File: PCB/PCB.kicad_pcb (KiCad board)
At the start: 2 copper layers, 266.7 x 76.2 mm, 122 parts, among them J1 USB-C USB 2.0 MC-372, J2 Conn_01x04, J3 Conn_01x02, Q1 AO3407, Q2 AO3406, SW1 SW_Push, SW10 SW_Push, SW11 SW_Push, SW12 SW_Push, SW13 SW_Push, SW14 SW_Push, SW15 SW_Push, SW16 SW_Push, SW17 SW_Push, SW18 SW_Push, SW19 SW_Push, SW2 SW_Push, SW20 SW_Push, SW21 SW_Push, SW22 SW_Push, SW23 SW_Push, SW24 SW_Push, SW25 SW_Push, SW26 SW_Push, SW27 SW_Push, SW28 SW_Push, SW29 SW_Push, SW3 SW_Push, SW30 SW_Push, SW31 SW_Push, SW32 SW_Push, SW33 SW_Push, SW34 SW_Push, SW35 SW_Push, SW36 SW_Push, SW37 SW_Push, SW38 SW_Push, SW39 SW_Push, SW4 SW_Push, SW40 SW_Push, SW41 SW_Push, SW42 SW_Push, SW43 SW_Push, SW44 SW_Push, SW45 SW_Push, SW46 SW_Push, SW47 SW_Push, SW48 SW_Push, SW49 SW_Push, SW5 SW_Push, SW50 SW_Push, SW51 MSK-12C02, SW6 SW_Push, SW7 SW_Push, SW8 SW_Push, SW9 SW_Push, U1 E73-2G4M08S1C, U2 MCP73831, U3 AP2112K-3.3

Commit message: Place diode
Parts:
- moved D15 425.9 mm to (34.9, 66.4), turned to 90 degrees
- moved D28 423.1 mm to (39.6, 85.5), turned to 90 degrees
- moved D16 404.6 mm to (56.3, 66.4), turned to 90 degrees
- moved D17 391.5 mm to (75.4, 66.4), turned to 90 degrees
- moved D18 366.7 mm to (94.4, 66.4), turned to 90 degrees
- moved D19 353.9 mm to (113.5, 66.4), turned to 90 degrees
- moved D20 329.2 mm to (132.5, 66.4), turned to 90 degrees
- moved D29 326.9 mm to (65.8, 85.5), turned to 90 degrees
- moved D41 294.9 mm to (56.3, 104.5), turned to 90 degrees
- moved D1 294.2 mm to (32.5, 47.4), turned to 90 degrees
- moved D9 281.6 mm to (184.9, 47.4), turned to 90 degrees
- moved D2 280.4 mm to (51.6, 47.4), turned to 90 degrees
- moved D3 272.2 mm to (70.6, 47.4), turned to 90 degrees
- moved D42 267.8 mm to (77.7, 104.5), turned to 90 degrees
- moved D30 263.1 mm to (84.9, 85.5), turned to 90 degrees
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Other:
- board size 266.7 x 76.2 mm -> 266.7 x 81.4 mm

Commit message: Place SMD components
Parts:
- D49, D50, D51, Q2, R1, R2, R4, R5, R6, R7, SW50, SW51: moved to B.Cu
- moved R5 499.1 mm to (28.6, 95.7)
- moved R4 496.8 mm to (32.1, 98.8), turned to 180 degrees
- moved U3 457.6 mm to (23.5, 106.9), turned to 270 degrees
- moved U2 454.7 mm to (27.3, 106.9), turned to 270 degrees
- moved Q1 448.1 mm to (31.2, 106.9), turned to 90 degrees
- moved R8 445.9 mm to (23.5, 111.9), turned to 180 degrees
- moved Q2 442.6 mm to (36.0, 97.3), turned to 180 degrees
- moved R7 435.7 mm to (32.1, 95.7)
- moved R6 371.5 mm to (21.5, 98.8), turned to 180 degrees
- moved C1 365.2 mm to (27.3, 110.1), turned to 180 degrees
- moved D49 364.2 mm to (25.0, 95.7)
- moved R1 363.7 mm to (21.5, 95.7)
- moved C3 363.4 mm to (23.5, 110.1), turned to 180 degrees
- moved R2 360.5 mm to (28.6, 98.8)
- moved D50 359.9 mm to (25.0, 98.8)
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
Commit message: Remove useless silkscreen
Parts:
- J3: footprint nrfmicro:connector_swd -> nrfmicro:connectro_bat; moved to B.Cu
- moved J3 41.8 mm to (34.9, 55.9), turned to 270 degrees
- moved SW51 29.1 mm to (16.1, 57.8)
- moved J2 24.9 mm to (42.6, 115.5)
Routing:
- added copper zone on B.Cu, net (none)
- added copper zone on F.Cu, net (none)
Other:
- board text added: "+"
- board text added: "-"
- board text added: "SWC"
- board text added: "SWD"

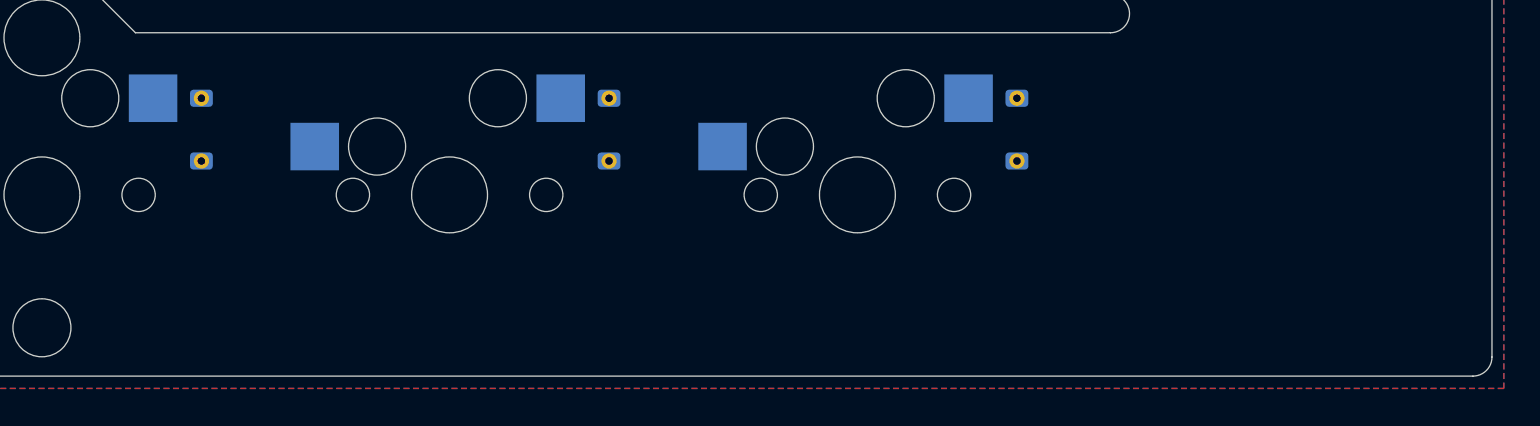
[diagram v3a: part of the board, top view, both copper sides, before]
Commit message: Edit footprints
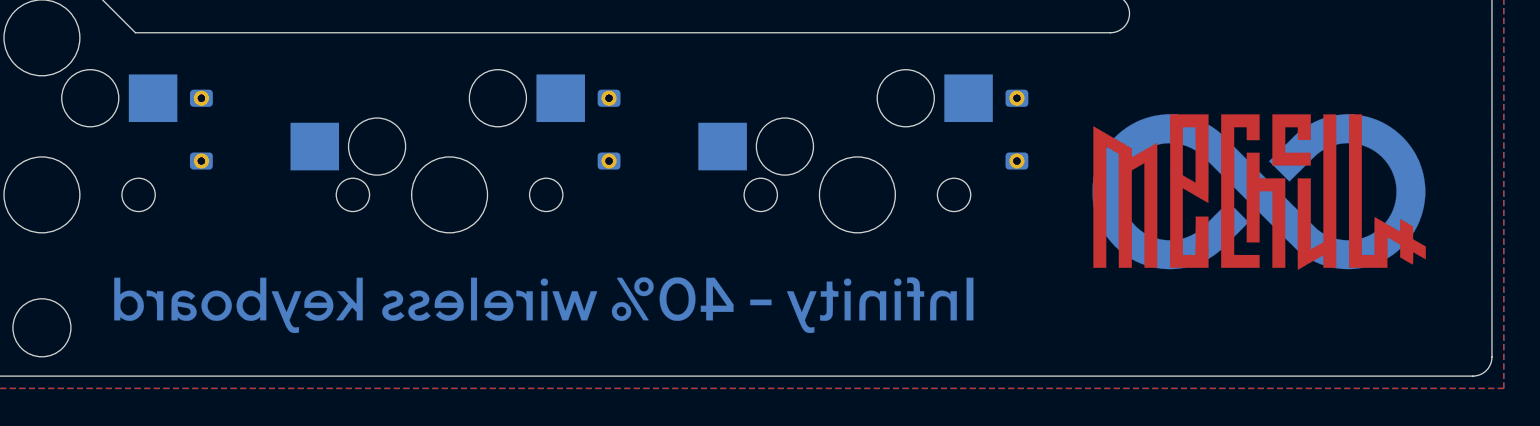
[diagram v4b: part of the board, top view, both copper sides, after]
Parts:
- added G***: LOGO, Infinity:InfinityText, B.Cu at (231.3, 113.7)
- added G***: LOGO, Infinity:InfinityLogo, B.Cu at (269.0, 107.8)
- added G***: LOGO, Infinity:MechCultLogo, F.Cu at (269.1, 107.8)

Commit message: Update route file
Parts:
- renumbered G*** to G1, G*** to G2, G*** to G3
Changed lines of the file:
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@@
   (module Infinity:InfinityText (layer B.Cu)
     (at 231.3178 113.7412 180)
-    (fp_text reference G*** (at 0 0) (layer B.SilkS) hide
+    (fp_text reference G3 (at 0 0) (layer B.SilkS) hide
       (effects (font (size 1.524 1.524) (thickness 0.3)) (justify mirror))
     )
@@
   (module Infinity:InfinityLogo (layer B.Cu)
     (at 269.0495 107.7976)
-    (fp_text reference G*** (at 0 0) (layer B.SilkS) hide
+    (fp_text reference G1 (at 0 0) (layer B.SilkS) hide
       (effects (font (size 1.524 1.524) (thickness 0.3)) (justify mirror))
     )
@@
   (module Infinity:MechCultLogo (layer F.Cu)
     (at 269.0876 107.7976)
-    (fp_text reference G*** (at 0 0) (layer F.SilkS) hide
+    (fp_text reference G2 (at 0 0) (layer F.SilkS) hide
       (effects (font (size 1.524 1.524) (thickness 0.3)))
     )
@@
     (at 34.8869 55.9308 270)
     (fp_text reference J3 (at 0 -1.7145 270) (layer Dwgs.User) hide
-      (effects (font (size 1 1) (thickness 0.15)) (justify mirror))
+      (effects (font (size 1 1) (thickness 0.15)))
     )
     (fp_text value Conn_01x02 (at 0 2.4765 270) (layer B.Fab) hide
@@
     (attr smd)
     (fp_text reference SW50 (at 0 3.75 90) (layer Dwgs.User) hide
-      (effects (font (size 1 1) (thickness 0.15)) (justify mirror))
+      (effects (font (size 1 1) (thickness 0.15)))
     )
     (fp_text value SW_Push (at 0 -3.75 90) (layer B.Fab) hide

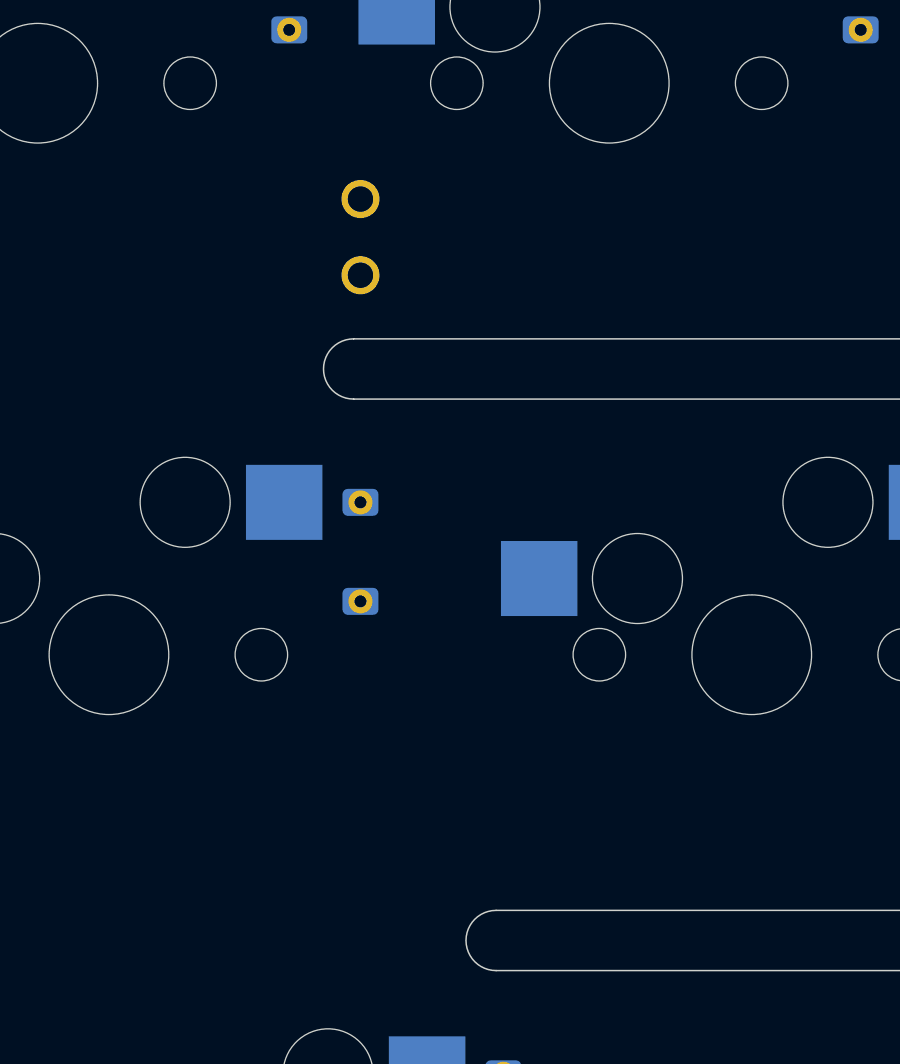
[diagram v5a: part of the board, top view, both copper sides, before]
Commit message: Move power ports
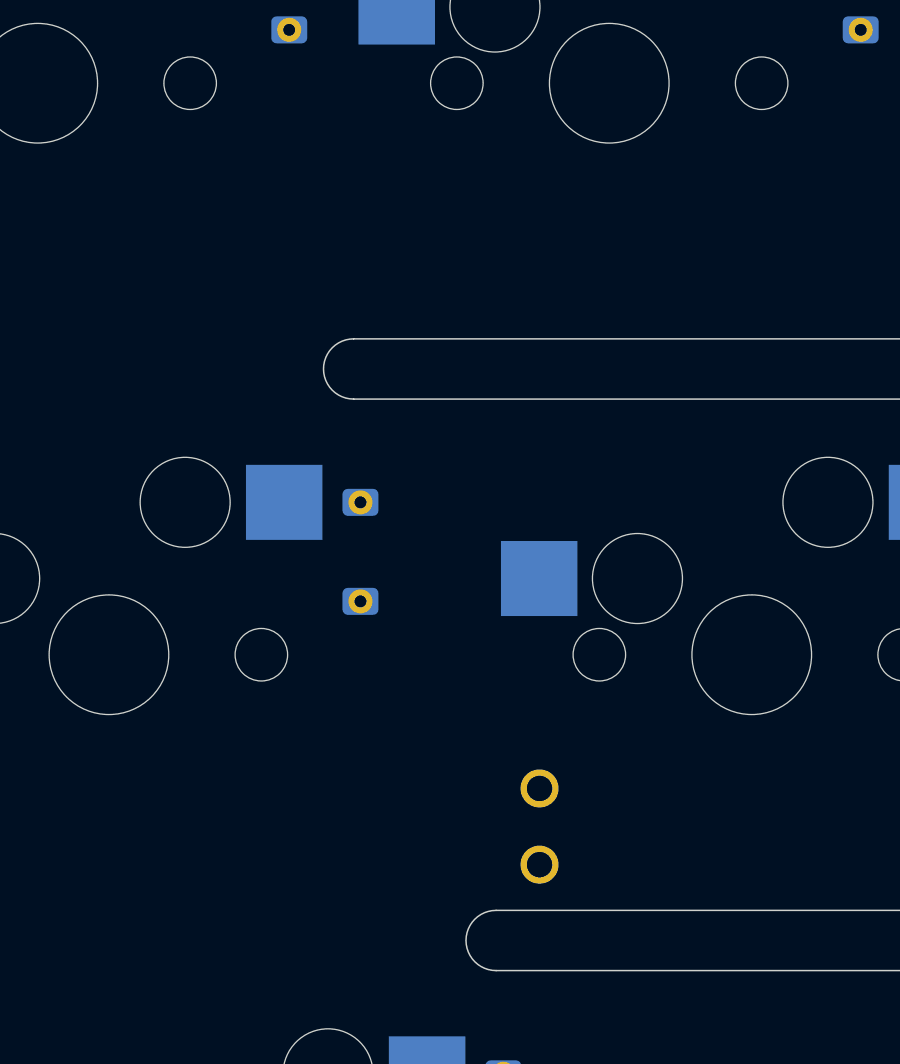
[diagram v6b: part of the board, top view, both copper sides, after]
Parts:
- moved J3 20.5 mm to (40.9, 75.6)
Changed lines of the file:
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@@
   )
   (module nrfmicro:connectro_bat (layer B.Cu)
-    (at 34.8869 55.9308 270)
+    (at 40.8559 75.5777 270)
     (fp_text reference J3 (at 0 -1.7145 270) (layer Dwgs.User) hide
       (effects (font (size 1 1) (thickness 0.15)))

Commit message: Route tracks
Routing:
- net /P0.02: track 0.00 -> 758.1 mm, vias 0 -> 13
- net /P0.30: track 0.00 -> 629.0 mm, vias 0 -> 6
- net /P0.00: track 0.00 -> 578.3 mm, vias 0 -> 7
- net /P1.04: track 0.00 -> 577.3 mm, vias 0 -> 4
- net /P0.29: track 0.00 -> 549.0 mm, vias 0 -> 12
- net /P0.31: track 0.00 -> 526.2 mm, vias 0 -> 2
- net /P0.01: track 0.00 -> 511.2 mm, vias 0 -> 4
- net /P0.05: track 0.00 -> 425.8 mm, vias 0 -> 4
- net /P0.10: track 0.00 -> 394.5 mm, vias 0 -> 2
- net /P0.12: track 0.00 -> 348.2 mm, vias 0 -> 5
- net SWO: track 0.00 -> 337.7 mm, vias 0 -> 4
- net /P0.24: track 0.00 -> 297.2 mm, vias 0 -> 2
- net /P0.09: track 0.00 -> 285.6 mm, vias 0 -> 2
- net /P1.13: track 0.00 -> 263.4 mm, vias 0 -> 16
- net /P0.22: track 0.00 -> 250.9 mm
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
